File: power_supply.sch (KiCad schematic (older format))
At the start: 9 parts

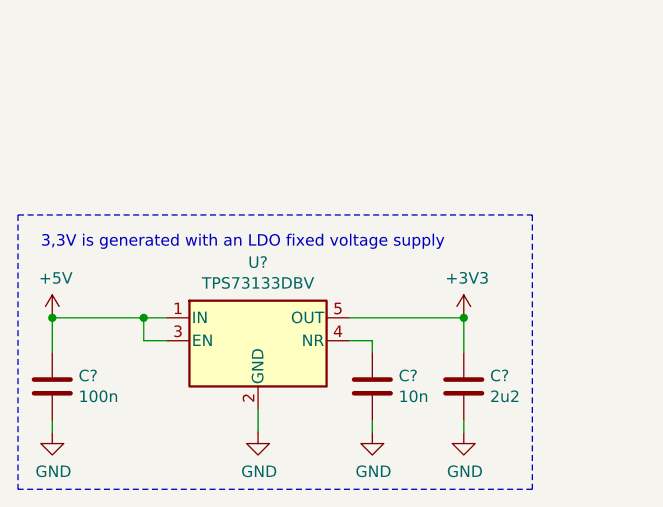
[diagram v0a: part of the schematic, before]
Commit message: Added RTC for timekeeping, AVR can now measure supply voltage.
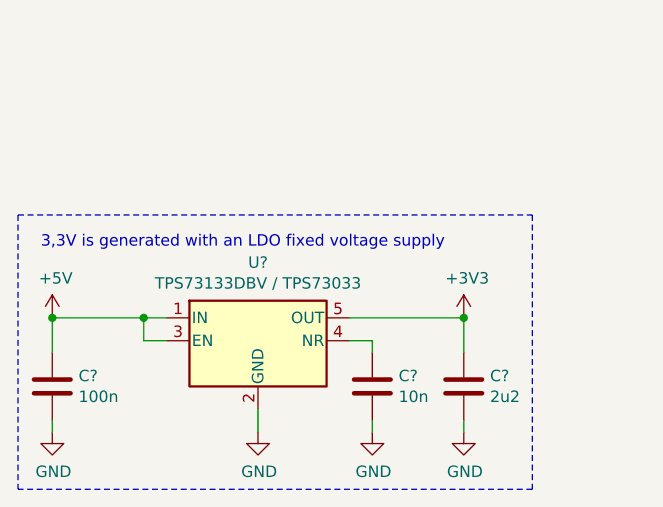
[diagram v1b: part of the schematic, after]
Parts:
- U?: value TPS73133DBV -> TPS73133DBV / TPS73033
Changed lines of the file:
@@
 P 3400 6000
 F 0 "U?" H 3400 6342 50  0000 C CNN
-F 1 "TPS73133DBV" H 3400 6251 50  0000 C CNN
+F 1 "TPS73133DBV / TPS73033" H 3400 6251 50  0000 C CNN
 F 2 "Package_TO_SOT_SMD:SOT-23-5" H 3400 6325 50  0001 C CIN
 F 3 "http://www.ti.com/lit/ds/symlink/tps731.pdf" H 3400 5950 50  0001 C CNN
